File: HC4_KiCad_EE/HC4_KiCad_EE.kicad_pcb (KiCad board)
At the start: 2 copper layers, 100 x 100 mm, 124 parts, among them IC1 74HC86, IC10 74HC161, IC11 74HC74, IC12 74HC00, IC13 74HC4053, IC14 74HC02, IC15 74HC14, IC2 74HC283, IC3 74HC253, IC4 74HC253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

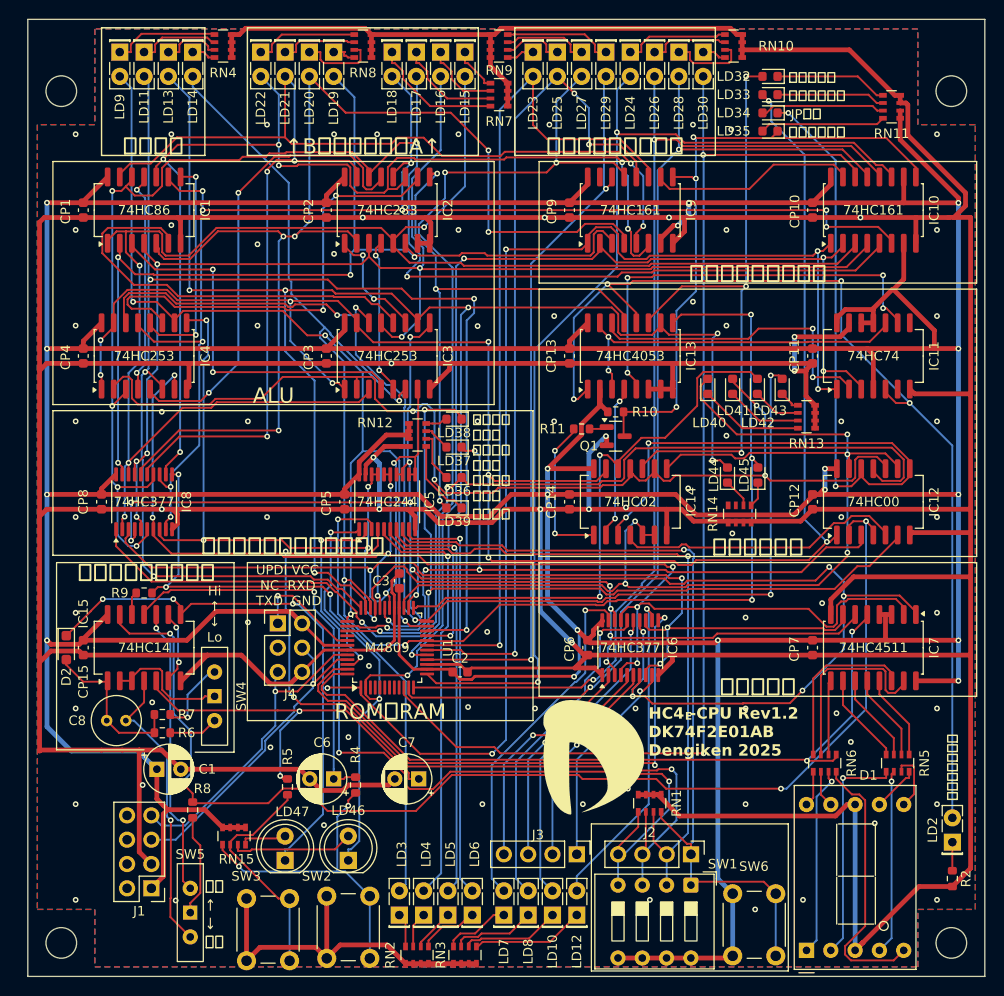
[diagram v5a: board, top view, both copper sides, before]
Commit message: MOSFETを回路上より排除
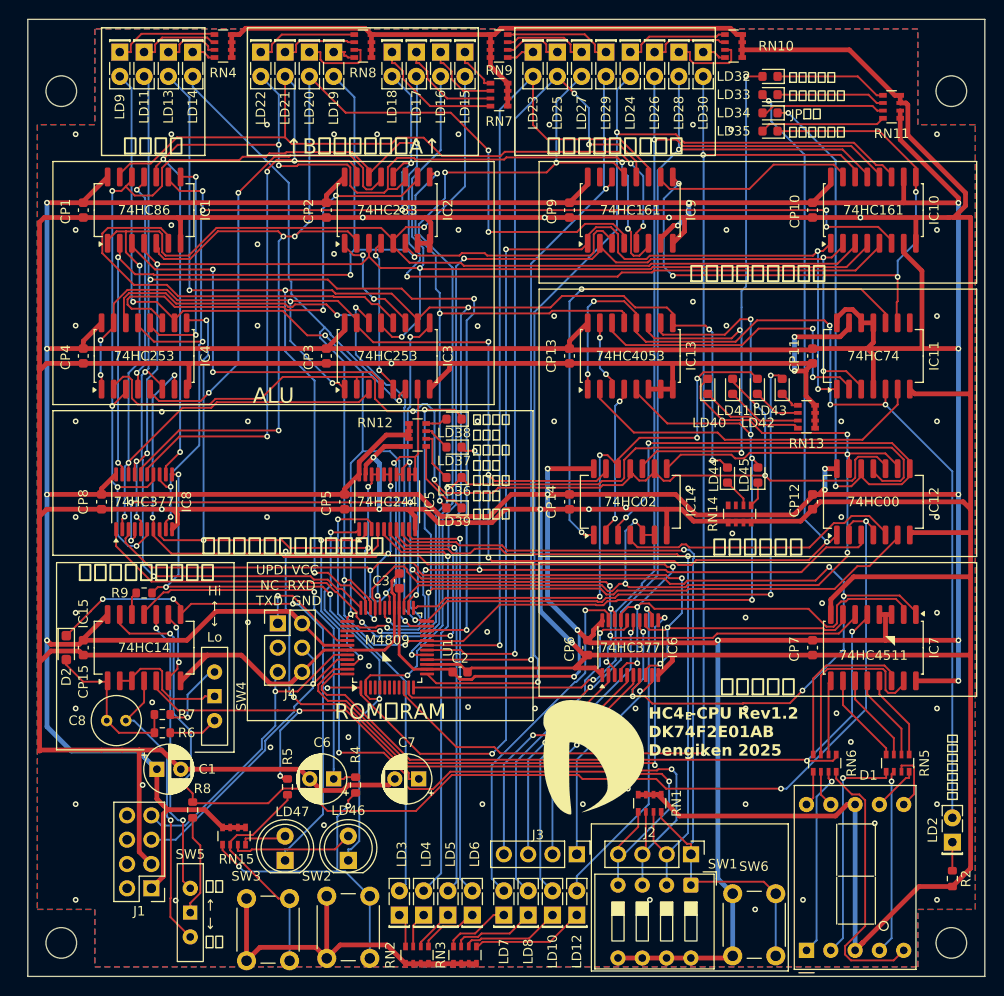
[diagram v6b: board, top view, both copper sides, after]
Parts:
- removed Q1: BSS138, Package_TO_SOT_SMD:SOT-23
- removed R10, R11: 1k, Resistor_SMD:R_0603_1608Metric
- D2: value D -> Schottky
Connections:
- IC11 pad 6: unconnected-(IC11A-~{Q}-Pad6) -> /Instruction Decoder/~{Carry_Flg}
- IC11 pad 9: Net-(IC11B-Q) -> /Instruction Decoder/~{JMP}
- IC13 pad 10: /ALU/Instruction_1 -> /ALU/Instruction_0
- IC13 pad 15: Net-(IC11B-~{S}) -> Net-(IC13-Y)
- IC13 pad 2: VCC -> /Instruction Decoder/~{Carry_Flg}
- IC13 pad 3: Net-(IC11B-~{S}) -> Net-(IC13-Y)
- IC13 pad 5: Net-(IC11B-Q) -> /ALU/Instruction_0
- IC13 pad 9: /ALU/Instruction_0 -> /ALU/Instruction_1
- IC14 pad 1: Net-(IC14-Pad1) -> Net-(IC11B-~{S})
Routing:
- net Net-(IC11B-Q): track 44.6 -> 0.00 mm, vias 4 -> 0
- net /Instruction Decoder/~{Carry_Flg}: track 0.00 -> 37.0 mm
- net Net-(IC11B-~{S}): track 37.7 -> 62.0 mm
- net /ALU/Instruction_0: track 165.7 -> 182.8 mm, vias 6 -> 7
- net VCC: track 725.8 -> 709.3 mm
- net Net-(IC14-Pad1): track 16.2 -> 0.00 mm, vias 2 -> 0
- net /Instruction Decoder/Carry_Flg: track 109.5 -> 99.9 mm, vias 4 -> 5
- net GND: track 890.1 -> 881.4 mm, vias 86 -> 84
- net Net-(IC13-Y): track 0.00 -> 7.45 mm, vias 0 -> 2
- net /ALU/Instruction_5: track 58.2 -> 60.9 mm, vias 2 -> 4
- net Net-(Q1-G): track 1.87 -> 0.00 mm
- net /Instruction Decoder/~{JMP}: track 66.5 -> 68.3 mm, vias 3 -> 4
- net /ALU/Carry_OUT: track 59.8 -> 58.6 mm
- net /Instruction Decoder/Carry_EN: track 64.6 -> 63.8 mm
- net /ALU/Instruction_1: track 175.4 -> 174.8 mm
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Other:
- board text added: "M4809 ◣"
- board text added: "◥ 74HC4511"
- board text removed: "74HC4511"
- board text removed: "M4809"

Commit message: 基板に反映
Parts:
- added J5: Expantion, Connector_PinHeader_2.54mm:PinHeader_2x06_P2.54mm_Vertical, F.Cu at (84.6, 137.2)
- moved C7 8.89 mm to (77.0, 134.6)
- moved C6 7.18 mm to (69.8, 134.6)
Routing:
- net /ALU/Instruction_3: track 102.7 -> 170.7 mm, vias 4 -> 7
- net /ALU/Instruction_1: track 174.8 -> 228.2 mm, vias 7 -> 8
- net /ALU/ALU_OUT2: track 139.7 -> 187.5 mm, vias 8 -> 13
- net /ALU/ALU_OUT1: track 174.1 -> 220.7 mm, vias 12 -> 9
- net /ALU/ALU_OUT3: track 133.5 -> 179.4 mm, vias 9 -> 12
- net Net-(IC5-1A3): track 88.7 -> 132.2 mm, vias 1 -> 6
- net /ALU/Instruction_2: track 152.9 -> 112.0 mm, vias 5 -> 7
- net /ALU/ALU_in_A1: track 143.7 -> 182.8 mm, vias 6 -> 8
- net /ALU/Instruction_7: track 119.8 -> 84.9 mm, vias 5 -> 8
- net /Instruction Decoder/~{RAM_RD}: track 76.4 -> 110.3 mm, vias 4 -> 5
- net /ALU/ALU_OUT0: track 130.1 -> 160.5 mm, vias 6 -> 13
- net GND: track 881.4 -> 852.1 mm, vias 84 -> 60
- net /Instruction Decoder/READ: track 187.2 -> 159.7 mm, vias 9 -> 8
- net /Instruction Decoder/~{RAM_WR}: track 88.1 -> 115.4 mm, vias 3 -> 7
- net /Program Counter/PC_3: track 110.4 -> 136.1 mm, vias 2 -> 5
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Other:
- board text added: "HC4 -CPU Rev2.0 DK74F2E01BB Dengiken 2026"
- board text removed: "HC4 -CPU Rev1.2 DK74F2E01AB Dengiken 2025"

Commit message: 配線のやり直しをやり直し
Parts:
- moved SW3 0.21 mm to (67.9, 153.2)
- moved SW2 0.06 mm to (76.2, 153.2)
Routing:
- net /ALU/Instruction_1: track 228.2 -> 0.00 mm, vias 8 -> 0
- net /ALU/ALU_OUT1: track 220.7 -> 0.00 mm, vias 9 -> 0
- net ~{RESET}: track 202.8 -> 0.00 mm, vias 10 -> 0
- net /ALU/Instruction_0: track 187.7 -> 0.00 mm, vias 11 -> 0
- net /ALU/ALU_OUT2: track 187.5 -> 0.00 mm, vias 13 -> 0
- net /ALU/ALU_in_A1: track 182.8 -> 0.00 mm, vias 8 -> 0
- net /ALU/ALU_OUT3: track 179.4 -> 0.00 mm, vias 12 -> 0
- net CLK: track 173.9 -> 0.00 mm, vias 9 -> 0
- net /ALU/Instruction_3: track 170.7 -> 0.00 mm, vias 7 -> 0
- net /ALU/ALU_OUT0: track 160.5 -> 0.00 mm, vias 13 -> 0
- net /Instruction Decoder/READ: track 159.7 -> 0.00 mm, vias 8 -> 0
- net /ALU/ALU_in_A0: track 155.0 -> 0.00 mm, vias 7 -> 0
- net /ALU/ALU_in_A3: track 151.8 -> 0.00 mm, vias 9 -> 0
- net /ALU/ALU_in_A2: track 148.5 -> 0.00 mm, vias 6 -> 0
- net /ALU/ALU_in_B2: track 143.4 -> 0.00 mm, vias 9 -> 0
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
